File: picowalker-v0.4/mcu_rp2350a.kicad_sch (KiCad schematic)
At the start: 33 parts, among them SW1 ~{BOOT}, SW2 RUN, U1 RP2350A-QFN60, Y1 ABM8-272-T3

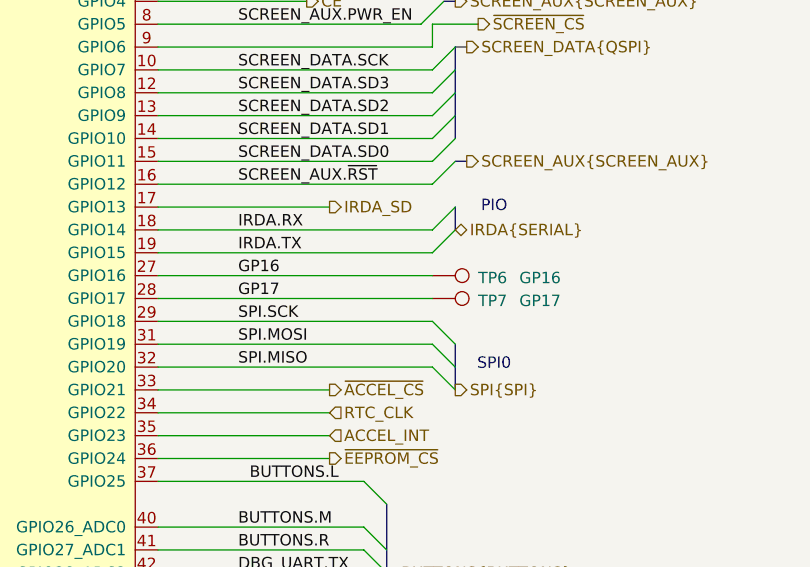
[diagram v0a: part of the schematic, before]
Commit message: v0.4: connect i2c to TP and add silkscreen labels
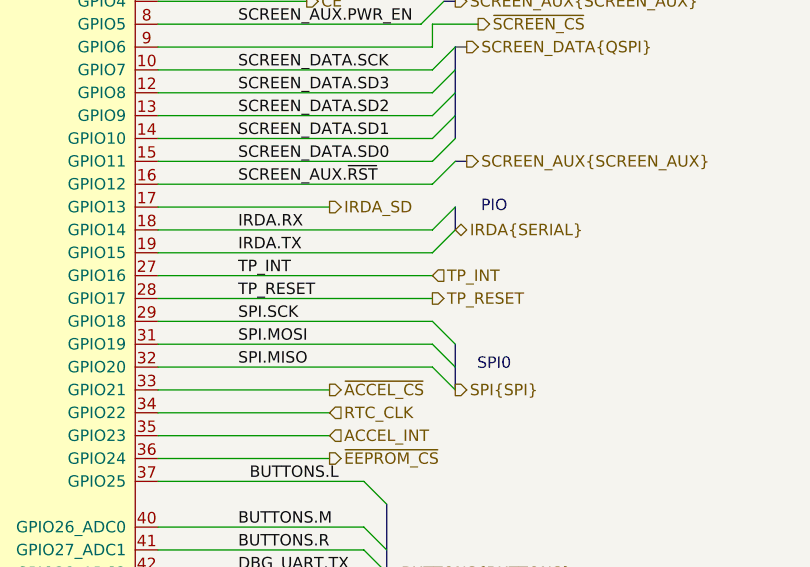
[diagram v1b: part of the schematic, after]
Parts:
- removed TP6: GP16, picowalker:TestPoint_Pad_D1.0mm_Nosilk, symbol Connector:TestPoint
- removed TP7: GP17, picowalker:TestPoint_Pad_D1.0mm_Nosilk, symbol Connector:TestPoint
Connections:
- net GP16 renamed TP_INT
- net GP17 renamed TP_RESET
